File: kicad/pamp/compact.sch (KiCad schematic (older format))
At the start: 99 parts, among them J1 input, J3 output, J4 power, Q10 BC546B, Q11 MJE340, Q12 2SA1381F, Q13 2SC3503F, Q14 BC546B, Q15 BC556B, Q3 2SA1381F, Q6 BC560C, Q8 BC560C, Q9 BC556B

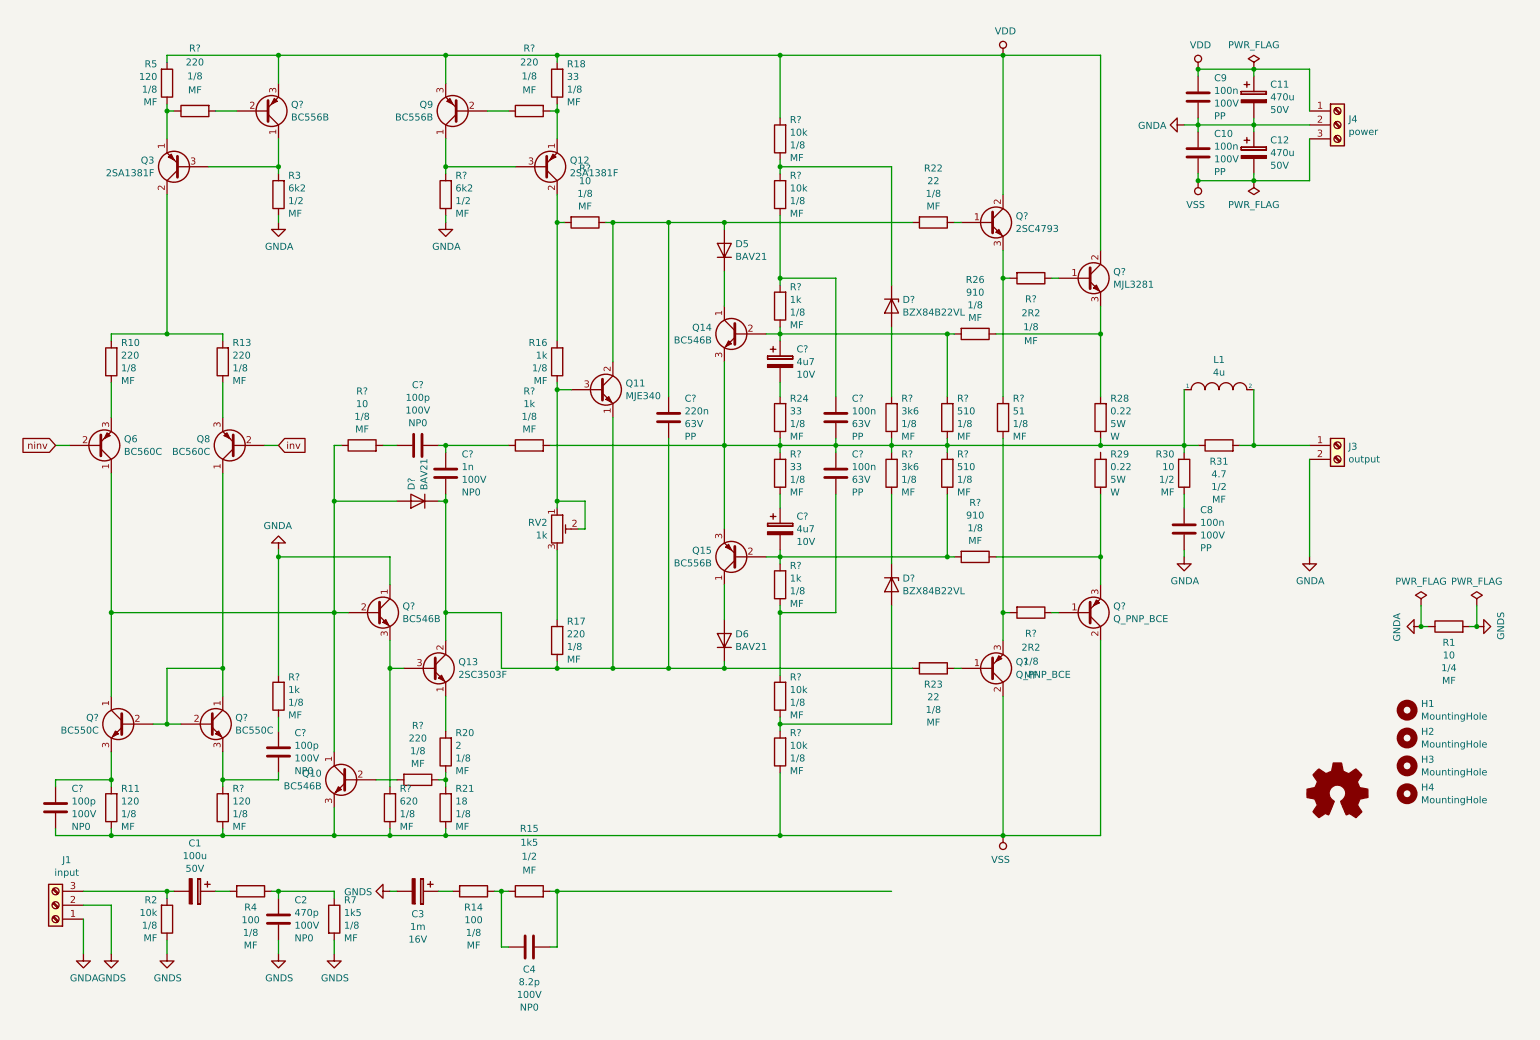
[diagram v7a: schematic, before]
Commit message: Minimal PCB version.
Signed-off-by: Nenad Radulovic <nenad.b.radulovic@gmail.com>
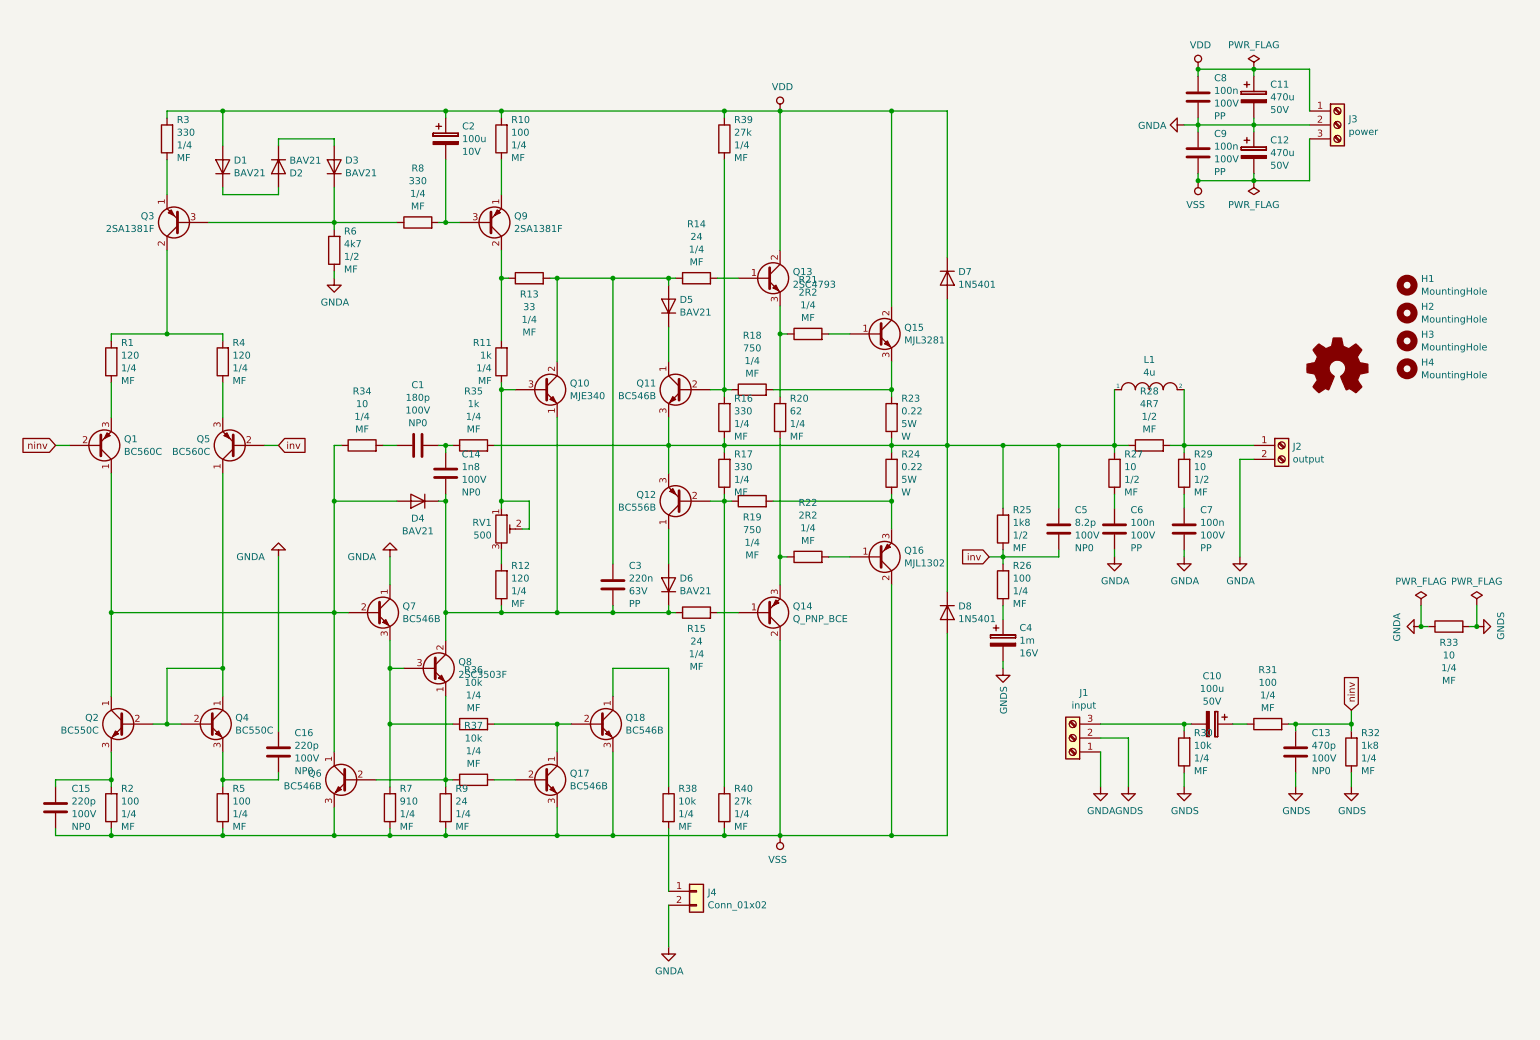
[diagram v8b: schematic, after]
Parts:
- removed C? (x2): 100p, Capacitor_THT:C_Disc_D8.0mm_W2.5mm_P5.00mm, symbol Device:C
- removed C? (x2): 4u7, Capacitor_THT:CP_Radial_D5.0mm_P2.50mm, symbol Device:CP
- removed C? (x2): 100n, Capacitor_THT:C_Rect_L7.2mm_W2.5mm_P5.00mm_FKS2_FKP2_MKS2_MKP2, symbol Device:C
- removed C?: 1n, Capacitor_THT:C_Disc_D8.0mm_W2.5mm_P5.00mm, symbol Device:C
- removed D? (x2): BZX84B22VL, Diode_THT:D_DO-41_SOD81_P7.62mm_Horizontal, symbol Device:D_Zener
- removed Q9, Q?: BC556B, Package_TO_SOT_THT:TO-92L_Inline, symbol Device:Q_PNP_CBE
- removed R1, R? (x2): 10, Resistor_THT:R_Axial_DIN0207_L6.3mm_D2.5mm_P10.16mm_Horizontal, symbol Device:R
- removed R23: 22, Resistor_THT:R_Axial_DIN0207_L6.3mm_D2.5mm_P10.16mm_Horizontal, symbol Device:R
- removed R24, R?: 33, Resistor_THT:R_Axial_DIN0207_L6.3mm_D2.5mm_P10.16mm_Horizontal, symbol Device:R
- removed R? (x3): 220, Resistor_THT:R_Axial_DIN0207_L6.3mm_D2.5mm_P10.16mm_Horizontal, symbol Device:R
- removed R?: 120, Resistor_THT:R_Axial_DIN0207_L6.3mm_D2.5mm_P10.16mm_Horizontal, symbol Device:R
- removed R?: 51, Resistor_THT:R_Axial_DIN0207_L6.3mm_D2.5mm_P10.16mm_Horizontal, symbol Device:R
- removed R? (x4): 1k, Resistor_THT:R_Axial_DIN0207_L6.3mm_D2.5mm_P10.16mm_Horizontal, symbol Device:R
- removed R? (x4): 10k, Resistor_THT:R_Axial_DIN0207_L6.3mm_D2.5mm_P10.16mm_Horizontal, symbol Device:R
- removed R? (x2): 3k6, Resistor_THT:R_Axial_DIN0207_L6.3mm_D2.5mm_P10.16mm_Horizontal, symbol Device:R
- removed R?: 620, Resistor_THT:R_Axial_DIN0207_L6.3mm_D2.5mm_P10.16mm_Horizontal, symbol Device:R
- removed R?: 6k2, Resistor_THT:R_Axial_DIN0411_L9.9mm_D3.6mm_P12.70mm_Horizontal, symbol Device:R
- removed R? (x2): 510, Resistor_THT:R_Axial_DIN0207_L6.3mm_D2.5mm_P10.16mm_Horizontal, symbol Device:R
- removed R?: 910, Resistor_THT:R_Axial_DIN0207_L6.3mm_D2.5mm_P10.16mm_Horizontal, symbol Device:R
- removed R? (x2): 2R2, Resistor_THT:R_Axial_DIN0207_L6.3mm_D2.5mm_P10.16mm_Horizontal, symbol Device:R
- added C14: 1n8, Capacitor_THT:C_Disc_D8.0mm_W2.5mm_P5.00mm, symbol Device:C
- added C15, C16: 220p, Capacitor_THT:C_Disc_D8.0mm_W2.5mm_P5.00mm, symbol Device:C
- added C2: 100u, Capacitor_THT:CP_Radial_D8.0mm_P2.50mm, symbol Device:CP
- added C7: 100n, Capacitor_THT:C_Rect_L7.2mm_W5.5mm_P5.00mm_FKS2_FKP2_MKS2_MKP2, symbol Device:C
- added D1, D2, D3: BAV21, Diode_THT:D_DO-41_SOD81_P7.62mm_Horizontal, symbol Device:D
- added D7, D8: 1N5401, Diode_THT:D_DO-201AD_P15.24mm_Horizontal, symbol Device:D
- added J4: Conn_01x02, Connector_PinHeader_2.54mm:PinHeader_1x02_P2.54mm_Vertical, symbol Connector_Generic:Conn_01x02
- added Q17, Q18: BC546B, Package_TO_SOT_THT:TO-92L_Inline, symbol Device:Q_NPN_CBE
- added R10: 100, Resistor_THT:R_Axial_DIN0207_L6.3mm_D2.5mm_P10.16mm_Horizontal, symbol Device:R
- added R12: 120, Resistor_THT:R_Axial_DIN0207_L6.3mm_D2.5mm_P10.16mm_Horizontal, symbol Device:R
- added R19: 750, Resistor_THT:R_Axial_DIN0207_L6.3mm_D2.5mm_P10.16mm_Horizontal, symbol Device:R
- added R25: 1k8, Resistor_THT:R_Axial_DIN0411_L9.9mm_D3.6mm_P12.70mm_Horizontal, symbol Device:R
- added R27, R29: 10, Resistor_THT:R_Axial_DIN0411_L9.9mm_D3.6mm_P12.70mm_Horizontal, symbol Device:R
- added R28: 4R7, Resistor_THT:R_Axial_DIN0411_L9.9mm_D3.6mm_P12.70mm_Horizontal, symbol Device:R
- added R32: 1k8, Resistor_THT:R_Axial_DIN0207_L6.3mm_D2.5mm_P10.16mm_Horizontal, symbol Device:R
- added R33, R34: 10, Resistor_THT:R_Axial_DIN0207_L6.3mm_D2.5mm_P10.16mm_Horizontal, symbol Device:R
- added R35: 1k, Resistor_THT:R_Axial_DIN0207_L6.3mm_D2.5mm_P10.16mm_Horizontal, symbol Device:R
- added R36, R37, R38: 10k, Resistor_THT:R_Axial_DIN0207_L6.3mm_D2.5mm_P10.16mm_Horizontal, symbol Device:R
- added R39, R40: 27k, Resistor_THT:R_Axial_DIN0207_L6.3mm_D2.5mm_P10.16mm_Horizontal, symbol Device:R
- added R6: 4k7, Resistor_THT:R_Axial_DIN0411_L9.9mm_D3.6mm_P12.70mm_Horizontal, symbol Device:R
- added R8: 330, Resistor_THT:R_Axial_DIN0207_L6.3mm_D2.5mm_P10.16mm_Horizontal, symbol Device:R
- added R9: 24, Resistor_THT:R_Axial_DIN0207_L6.3mm_D2.5mm_P10.16mm_Horizontal, symbol Device:R
- C1: renamed from C?; value 100p -> 180p
- C13: renamed from C2; footprint Capacitor_THT:C_Disc_D3.8mm_W2.6mm_P2.50mm -> Capacitor_THT:C_Disc_D8.0mm_W2.5mm_P5.00mm
- J2: renamed from J3; footprint TerminalBlock_Phoenix:TerminalBlock_Phoenix_MKDS-1,5-2_1x02_P5.00mm_Horizontal -> Connector_Phoenix_MC:PhoenixContact_MCV_1,5_2-G-3.81_1x02_P3.81mm_Vertical
- J3: renamed from J4; footprint TerminalBlock_Phoenix:TerminalBlock_Phoenix_MKDS-1,5-3-5.08_1x03_P5.08mm_Horizontal -> Connector_Phoenix_MC:PhoenixContact_MCV_1,5_3-G-3.81_1x03_P3.81mm_Vertical
- Q14: renamed from Q?; footprint (none) -> Package_TO_SOT_THT:TO-220-3_Vertical
- Q15: renamed from Q?; footprint Package_TO_SOT_THT:TO-220-3_Vertical -> Package_TO_SOT_THT:TO-264-3_Vertical
- Q16: renamed from Q?; value Q_PNP_BCE -> MJL1302; footprint (none) -> Package_TO_SOT_THT:TO-264-3_Vertical
- Q8: renamed from Q13; footprint Package_TO_SOT_THT:TO-126-3_Vertical -> Package_TO_SOT_THT:TO-126-3_Horizontal_TabDown
- Q9: renamed from Q12; footprint Package_TO_SOT_THT:TO-126-3_Vertical -> Package_TO_SOT_THT:TO-126-3_Horizontal_TabDown
- R1: renamed from R10; value 220 -> 120; Manufacturer1 (none) -> Multicomp: MF25 120R; Power 1/8 -> 1/4; Supplier1A: (none) -> Farnell: 9341218
- R11: value 120 -> 1k; Manufacturer1 (none) -> Multicomp: MF25 1k; Power 1/8 -> 1/4; Supplier1A: (none) -> Farnell: 9341102
- R13: value 220 -> 33; Manufacturer1 (none) -> Multicomp: MF25 33R; Power 1/8 -> 1/4; Supplier1A: (none) -> Farnell: 9341773
- R14: value 100 -> 24; Manufacturer1 (none) -> Multicomp: MF25 24R; Power 1/8 -> 1/4; Supplier1A: (none) -> Farnell: 9341625
- R15: value 1k5 -> 24; footprint Resistor_THT:R_Axial_DIN0411_L9.9mm_D3.6mm_P12.70mm_Horizontal -> Resistor_THT:R_Axial_DIN0207_L6.3mm_D2.5mm_P10.16mm_Horizontal; Manufacturer1 (none) -> Multicomp: MF25 24R; Power 1/2 -> 1/4; Supplier1A: (none) -> Farnell: 9341625
- R16: value 1k -> 330; Manufacturer1 (none) -> Multicomp: MF25 330R; Power 1/8 -> 1/4; Supplier1A: (none) -> Farnell: 9341730
- R17: value 220 -> 330; Manufacturer1 (none) -> Multicomp: MF25 330R; Power 1/8 -> 1/4; Supplier1A: (none) -> Farnell: 9341730
- R18: value 33 -> 750; Manufacturer1 (none) -> Multicomp: MF25 1k; Power 1/8 -> 1/4; Supplier1A: (none) -> Farnell:
- R2: value 10k -> 100; Manufacturer1 (none) -> Multicomp: MF25 100R; Power 1/8 -> 1/4; Supplier1A: (none) -> Farnell: 9341099
- R20: value 2 -> 62; Manufacturer1 (none) -> Multicomp: MF25 62R; Power 1/8 -> 1/4; Supplier1A: (none) -> Farnell: 9342141
- R21: value 18 -> 2R2; Manufacturer1 (none) -> Multicomp: MF25 2R2; Power 1/8 -> 1/4; Supplier1A: (none) -> Farnell: 9341579
- R22: value 22 -> 2R2; Manufacturer1 (none) -> Multicomp: MF25 2R2; Power 1/8 -> 1/4; Supplier1A: (none) -> Farnell: 9341579
- R23: renamed from R28; footprint Resistor_THT:R_Box_L14.0mm_W5.0mm_P9.00mm -> Resistor_THT:R_Axial_Power_L20.0mm_W6.4mm_P25.40mm
- R24: renamed from R29; footprint Resistor_THT:R_Box_L14.0mm_W5.0mm_P9.00mm -> Resistor_THT:R_Axial_Power_L20.0mm_W6.4mm_P25.40mm
- R26: value 910 -> 100; Manufacturer1 (none) -> Multicomp: MF25 100R; Power 1/8 -> 1/4; Supplier1A: (none) -> Farnell: 9341099
- R3: value 6k2 -> 330; footprint Resistor_THT:R_Axial_DIN0411_L9.9mm_D3.6mm_P12.70mm_Horizontal -> Resistor_THT:R_Axial_DIN0207_L6.3mm_D2.5mm_P10.16mm_Horizontal; Manufacturer1 (none) -> Multicomp: MF25 330R; Power 1/2 -> 1/4; Supplier1A: (none) -> Farnell: 9341730
- R30: value 10 -> 10k; footprint Resistor_THT:R_Axial_DIN0411_L9.9mm_D3.6mm_P12.70mm_Horizontal -> Resistor_THT:R_Axial_DIN0207_L6.3mm_D2.5mm_P10.16mm_Horizontal; Manufacturer1 (none) -> Multicomp: MF25 10K; Power 1/2 -> 1/4; Supplier1A: (none) -> Farnell: 9341110
- R31: value 4.7 -> 100; footprint Resistor_THT:R_Axial_DIN0411_L9.9mm_D3.6mm_P12.70mm_Horizontal -> Resistor_THT:R_Axial_DIN0207_L6.3mm_D2.5mm_P10.16mm_Horizontal; Manufacturer1 (none) -> Multicomp: MF25 100R; Power 1/2 -> 1/4; Supplier1A: (none) -> Farnell: 9341099
- R4: value 100 -> 120; Manufacturer1 (none) -> Multicomp: MF25 120R; Power 1/8 -> 1/4; Supplier1A: (none) -> Farnell: 9341218
- R5: value 120 -> 100; Manufacturer1 (none) -> Multicomp: MF25 100R; Power 1/8 -> 1/4; Supplier1A: (none) -> Farnell: 9341099
- R7: value 1k5 -> 910; Manufacturer1 (none) -> Multicomp: MF25 910R; Power 1/8 -> 1/4; Supplier1A: (none) -> Farnell: 9342311
- RV1: renamed from RV2; value 1k -> 500
- gave numbers to parts that had none: 6
- renumbered C1 to C10, C3 to C4, C4 to C5, C8 to C6, C9 to C8, C10 to C9, Q6 to Q1, Q11 to Q10, Q14 to Q11, Q15 to Q12, Q8 to Q5, Q10 to Q6
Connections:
- net GNDA: now also C16.2, C7.2, J4.2 (Pin_2), R33.1, R6.1; no longer R3.1
- net GNDS: now also R30.1, R32.1, R33.2; no longer R2.1, R7.2
- net VDD: now also R3.2, C2.1, D1.2 (A), D7.1 (K), R10.2, R39.1; no longer R18.2, R5.2
- net VSS: now also R2.1, R5.1, R7.1, C15.1, D8.2 (A), Q17.3 (E), Q18.3 (E), R40.2, R9.2; no longer R11.1, R21.1
- net inv: now also C5.2, R26.2, R25.1
- net ninv: now also C13.2, R31.2, R32.2
- net at Q13.1 (B): now also R14.2; no longer R22.1
- net at C3.1, D5.2 (A), Q10.2 (C): now also R13.2, R14.1; no longer R22.2
- net at L1.1, Q11.3 (E), Q12.3 (E)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: now also C5.1, R16.1, R17.2, R24.2, D7.2 (A), D8.1 (K), R25.2, R27.2, R28.1, R35.2; no longer R30.2, R31.1
- net at Q15.3 (E), R23.2: now also R18.2; no longer R26.1
- net at Q16.3 (E), R24.1: now also R19.2
- net at Q14.1 (B): now also R15.2
- net at C3.2, D4.1 (K), D6.1 (K)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: now also R15.1, C14.1, R12.1; no longer R17.1
- net at Q11.2 (B): now also R16.2, R18.1, R39.2; no longer R26.2
- net at Q12.2 (B): now also R17.1, R19.1, R40.1
- net at Q10.3 (B), RV1.1, RV1.2: now also R11.1; no longer R16.1
- net at Q9.2 (C): now also R11.2, R13.1; no longer R16.2
- net at RV1.3: now also R12.2; no longer R17.2
- net at Q8.1 (E): now also Q6.2 (B), R37.1, R9.1; no longer R20.2
- net at Q7.3 (E), Q8.3 (B): now also R7.2, R36.1
- net at D4.2 (A), Q1.1 (C), Q2.1 (C)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: now also R34.1
- net at Q9.1 (E): now also R10.1; no longer R18.1
- net at Q9.3 (B): now also C2.2, R8.2
- net at R20.1: now also Q14.3 (E), R22.1; no longer R21.2
- net at Q5.3 (E): now also R4.1; no longer R13.1
- net at Q2.3 (E): now also R2.2, C15.2; no longer R11.2
- net at Q13.3 (E): now also R20.2, R21.1
- net at Q3.2 (C), R1.2: now also R4.2; no longer R13.2
- net at Q3.3 (B): now also D3.1 (K), R6.2, R8.1; no longer R3.2
- net at Q3.1 (E): now also R3.1; no longer R5.1
- net at Q4.3 (E): now also R5.2, C16.1
- net at C1.1: now also C14.2, R35.1
- net at C1.2: now also R34.2
- net at C4.1: now also R26.1; no longer R14.2
- net at C10.1: now also R31.1; no longer R4.2
- net at C10.2, J1.3 (Pin_3): now also R30.2; no longer R2.2
- net at C6.1: now also R27.1; no longer R30.1
- net at Q15.1 (B): now also R21.2
- net at Q16.1 (B): now also R22.2
- net at J2.1 (Pin_1), L1.2: now also R28.2, R29.2; no longer R31.2
- new net: D1.1 (K), D2.2 (A)
- new net: C7.1, R29.1
- new net: D2.1 (K), D3.2 (A)
- new net: Q17.1 (C), Q18.2 (B), R36.2
- new net: Q17.2 (B), R37.2
- new net: Q18.1 (C), R38.1
- new net: J4.1 (Pin_1), R38.2
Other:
- moved on the sheet: C10, C13, C3, C4, C5, C6, D5, D6, H1, H2, H3, H4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
